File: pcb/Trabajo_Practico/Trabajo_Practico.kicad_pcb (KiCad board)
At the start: 2 copper layers, 71.6 x 60.5 mm, 24 parts, among them J1 Conn_02x19_Odd_Even, J2 Conn_02x19_Odd_Even, J3 Conn_01x03_Male, J4 Conn_01x03_Male, J5 SD_Card_P, U1 ESP8266-01_ESP-01, U2 MAX30102_P, U4 DS18B20

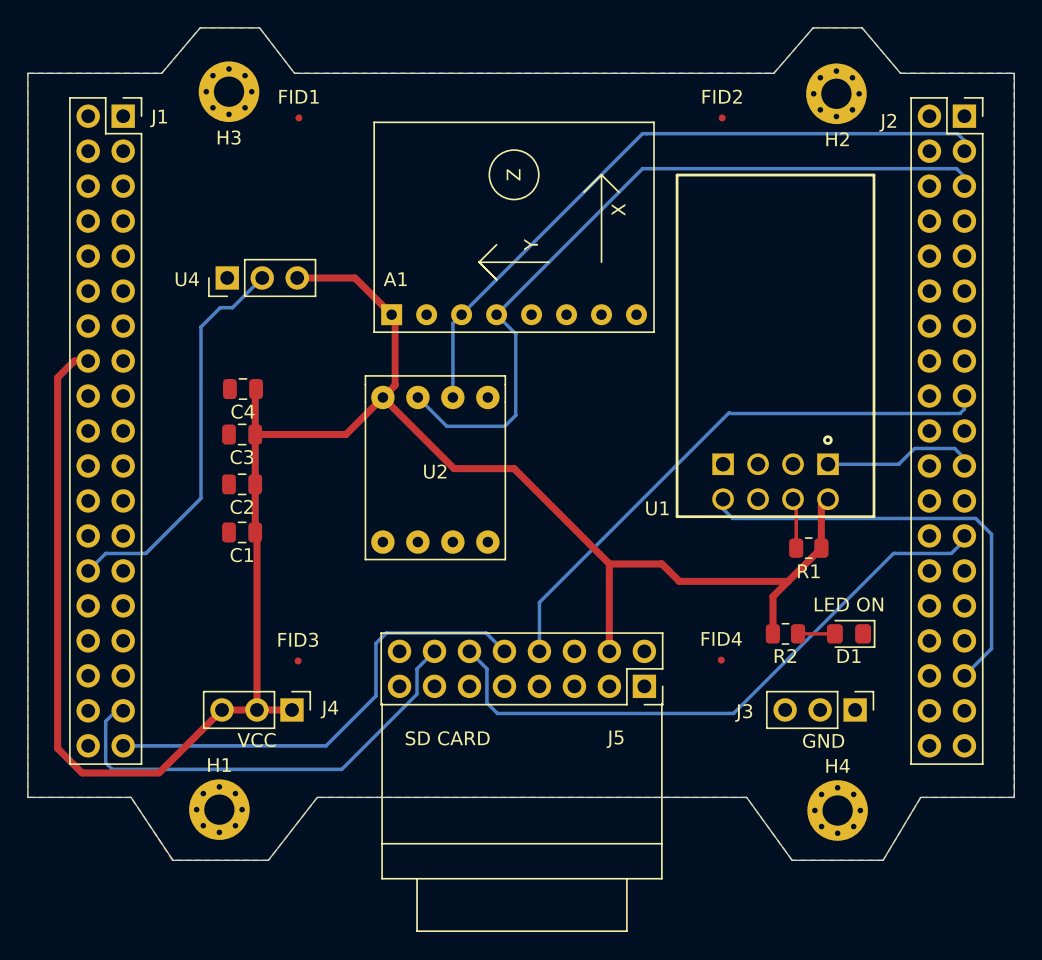
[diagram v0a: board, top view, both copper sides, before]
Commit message: Agrego sensor MLX90614
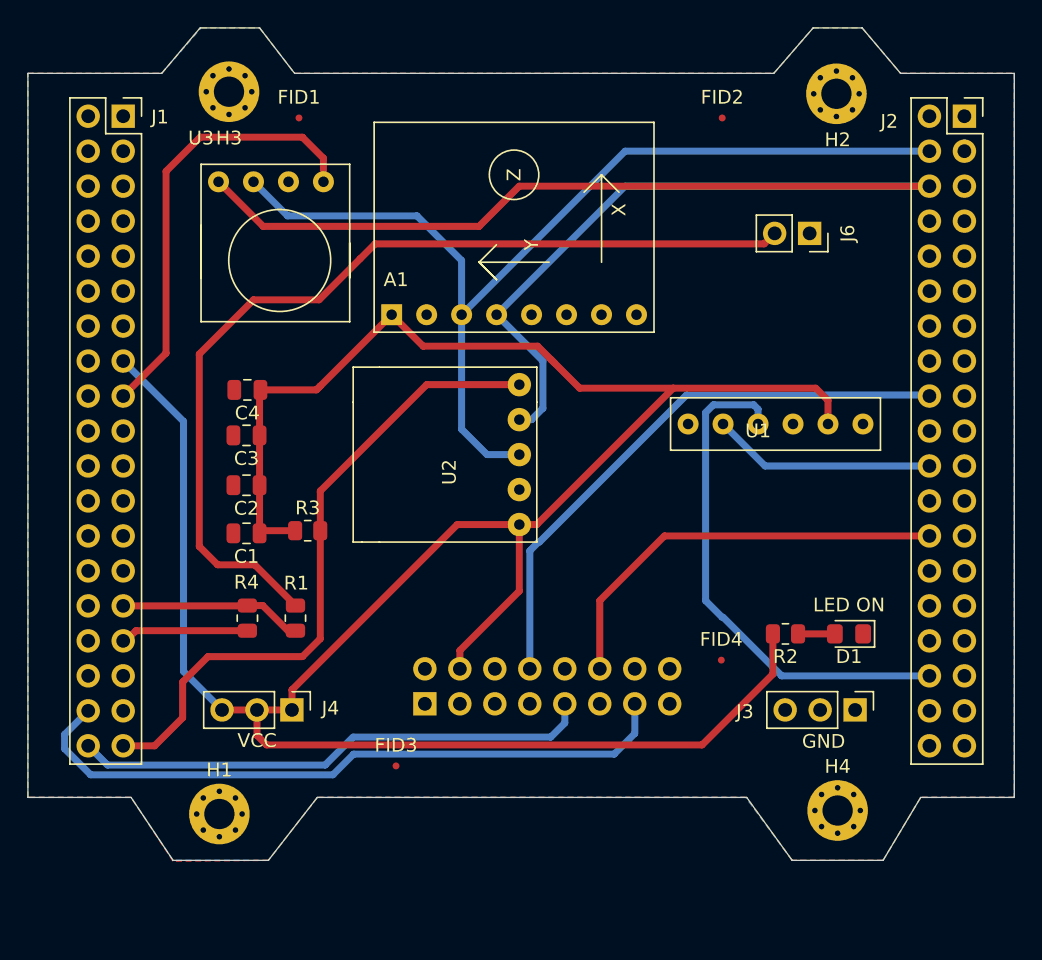
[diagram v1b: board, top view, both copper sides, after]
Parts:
- removed U4: DS18B20, Connector_PinHeader_2.54mm:PinHeader_1x03_P2.54mm_Vertical
- added J6: Conn_01x02_Female, Connector_PinSocket_2.54mm:PinSocket_1x02_P2.54mm_Vertical, F.Cu at (157.5, 71.9)
- added R3: 10k, Resistor_SMD:R_0805_2012Metric, F.Cu at (121.0, 93.5)
- added R4: 1k, Resistor_SMD:R_0805_2012Metric, F.Cu at (116.6, 99.9)
- added U3: MLX90614, TP_Footprints:MLX90614, F.Cu at (114.6, 68.2)
- J5: moved to B.Cu
- R1: value 10k -> 1k
- U1: value ESP8266-01_ESP-01 -> Tiny_Fox; footprint TP_Footprints:ESP-01 -> TP_Footprints:TinyFox
- U2: value MAX30102_P -> MAX30102_P-max30102
- moved R1 37.6 mm to (120.1, 99.9), turned to 90 degrees
- moved J5 16.0 mm to (129.5, 106.1)
- moved FID3 10.4 mm to (127.4, 110.6)
- moved U2 7.98 mm to (136.4, 88.0), turned to 270 degrees
- moved U1 3.19 mm to (153.7, 85.8), turned to 0 degrees
- moved C4 0.32 mm to (116.6, 83.3)
- moved C1 0.32 mm to (116.6, 93.7)
- moved C2 0.32 mm to (116.6, 90.2)
- moved C3 0.32 mm to (116.6, 86.6)
- moved H1 0.32 mm to (114.6, 114.1)
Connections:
- J1 pad 1: /PC10 -> /PC11
- J1 pad 11: Net-(J1-Pad11) -> /IOREF
- J1 pad 12: /IOREF -> Net-(J1-Pad12)
- J1 pad 13: /PA13 -> /RESET
- J1 pad 14: /RESET -> /PA13
- J1 pad 15: /PA14 -> VCC
- J1 pad 16: VCC -> /PA14
- J1 pad 17: /PA15 -> /+5V
- J1 pad 18: /+5V -> /PA15
- J1 pad 2: /PC11 -> /PC10
- J1 pad 21: /PB7 -> GND
- J1 pad 22: GND -> /PB7
- J1 pad 23: /PC13 -> /VIN
- J1 pad 24: /VIN -> /PC13
- J1 pad 25: /PC14 -> Net-(J1-Pad25)
- J1 pad 26: Net-(J1-Pad26) -> /PC14
- J1 pad 27: /PC15 -> /PA0
- J1 pad 28: /AN0 -> /PC15
- J1 pad 29: /PH0 -> /AN1
- J1 pad 3: /PC12 -> /PD2
- J1 pad 30: /PA1 -> /PH0
- J1 pad 31: /PH1 -> /M_BAT
- J1 pad 32: /PA4 -> /PH1
- J1 pad 33: /VBAT -> /PB0
- J1 pad 34: /PB0 -> /VBAT
- J1 pad 35: /MISO -> /PC1
- J1 pad 36: /PC1 -> /MISO
- J1 pad 37: /MOSI -> /PC0
- J1 pad 38: /PC0 -> /MOSI
- J1 pad 4: /PD2 -> /PC12
- J1 pad 5: /VDD -> /E5V
- J1 pad 6: /E5V -> /VDD
- J1 pad 7: /BOT0 -> GND
- J1 pad 8: GND -> /BOT0
- J2 pad 1: /PC9 -> /PC8
- J2 pad 10: Net-(J2-Pad10) -> GND
- J2 pad 11: /PA5 -> /PA12
- J2 pad 12: /PA12 -> /PA5
- J2 pad 13: /PA6 -> /PA11
- J2 pad 14: /PA11 -> /PA6
- J2 pad 15: /PA7 -> /PB12
- J2 pad 16: /PB12 -> /PA7
- J2 pad 17: /CS -> Net-(J2-Pad17)
- J2 pad 18: Net-(J2-Pad18) -> /CS
- J2 pad 19: /PC7 -> GND
- J2 pad 2: /PC8 -> /PC9
- J2 pad 20: GND -> /PC7
- J2 pad 21: /PA9 -> /PB2
- J2 pad 22: /PB2 -> /PA9
- J2 pad 23: /PA8 -> /PB1
- J2 pad 24: /PB1 -> /PA8
- J2 pad 25: /CLK -> /PB15
- J2 pad 26: /PB15 -> /CLK
- J2 pad 27: /PB4 -> /PB14
- J2 pad 28: /PB14 -> /PB4
- J2 pad 29: /PB5 -> /PB13
- J2 pad 3: /PB8 -> /PC6
- J2 pad 30: /PB13 -> /PB5
- J2 pad 31: /PB3 -> /AGND
- J2 pad 32: /AGND -> /PB3
- J2 pad 33: /PA10 -> /PC4
- J2 pad 34: /PC4 -> /PA10
- J2 pad 35: /PA2 -> Net-(J2-Pad35)
- J2 pad 36: Net-(J2-Pad36) -> /PA2
- J2 pad 37: /PA3 -> Net-(J2-Pad37)
- J2 pad 38: Net-(J2-Pad38) -> /PA3
- J2 pad 4: /PC6 -> /PB8
- J2 pad 5: /PB9 -> /PC5
- J2 pad 6: /PC5 -> /PB9
- J2 pad 7: /AVDD -> /U5V
- J2 pad 8: /U5V -> /AVDD
- J2 pad 9: GND -> Net-(J2-Pad9)
- J5 pad 13: Net-(J5-Pad13) -> /MOSI
- J5 pad 15: Net-(J5-Pad15) -> /MISO
- J5 pad 5: /MOSI -> Net-(J5-Pad5)
- J5 pad 7: /MISO -> Net-(J5-Pad7)
- R1 pad 1: Net-(R1-Pad1) -> /AN1
- R1 pad 2: VCC -> Net-(J6-Pad2)
- U1 pad 1: /PA9 -> GND
- U1 pad 2: Net-(U1-Pad2) -> /PA9
- U1 pad 3: Net-(U1-Pad3) -> /PA10
- U1 pad 4: GND -> Net-(U1-Pad4)
- U1 pad 5: /PA10 -> VCC
- U1 pad 6: Net-(U1-Pad6) -> GND
- U2 pad 1: GND -> VCC
- U2 pad 2: Net-(U2-Pad2) -> GND
- U2 pad 3: Net-(U2-Pad3) -> /PB8
- U2 pad 4: Net-(U2-Pad4) -> /PB9
- U2 pad 5: GND -> /PC0
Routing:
- net Net-(J6-Pad2): track 0.00 -> 68.1 mm
- net /PC0: track 0.00 -> 47.4 mm
- net /PB9: track 55.5 -> 99.7 mm
- net VCC: track 151.1 -> 192.3 mm
- net /+5V: track 0.00 -> 32.4 mm
- net /AN0: track 28.7 -> 0.00 mm
- net /PB8: track 49.2 -> 73.6 mm
- net /MISO: track 33.5 -> 49.0 mm
- net /CLK: track 44.8 -> 30.8 mm
- net /AN1: track 0.00 -> 13.3 mm
- net /M_BAT: track 0.00 -> 9.32 mm
- net /PA10: track 32.1 -> 37.7 mm
- net /PA9: track 11.6 -> 16.4 mm
- net /MOSI: track 33.9 -> 37.8 mm
- net Net-(R1-Pad1): track 3.65 -> 0.00 mm
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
